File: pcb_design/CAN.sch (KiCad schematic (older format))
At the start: 7 parts, among them U2 ISO1050

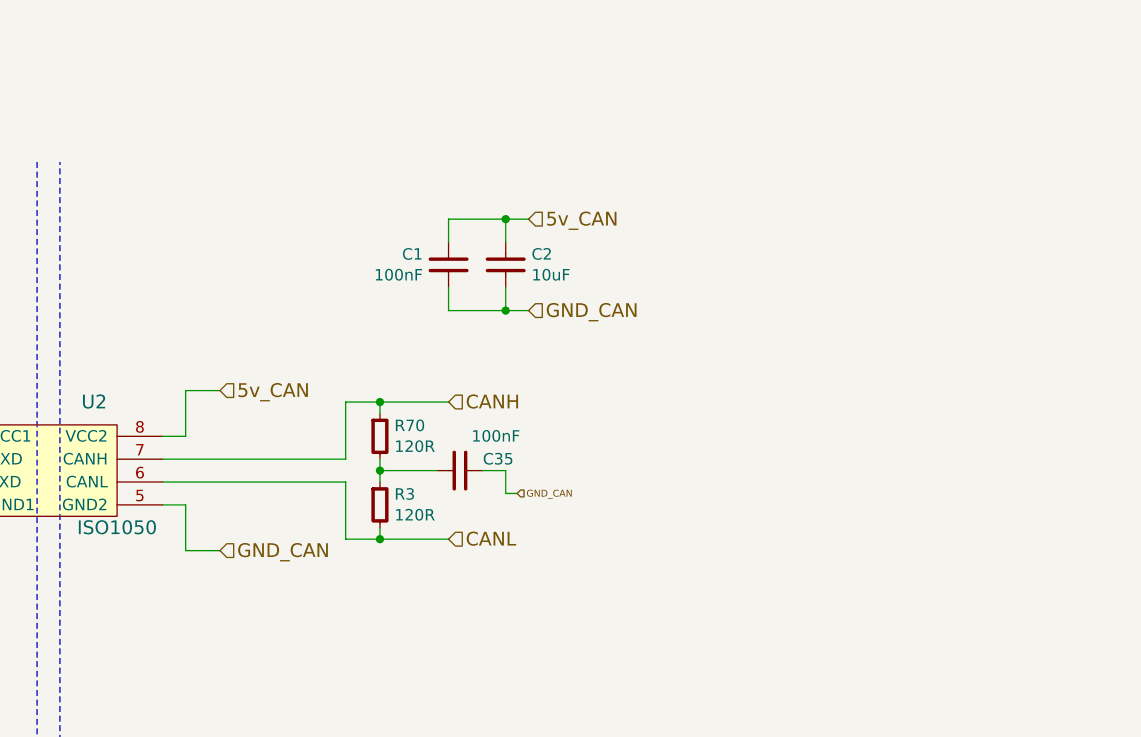
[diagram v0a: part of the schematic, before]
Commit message: Added reverse polarity protection on the isolated side of CON connector. Also, more layout
Signed-off-by: Marcos Chaparro <mchaparro@paltatech.com>
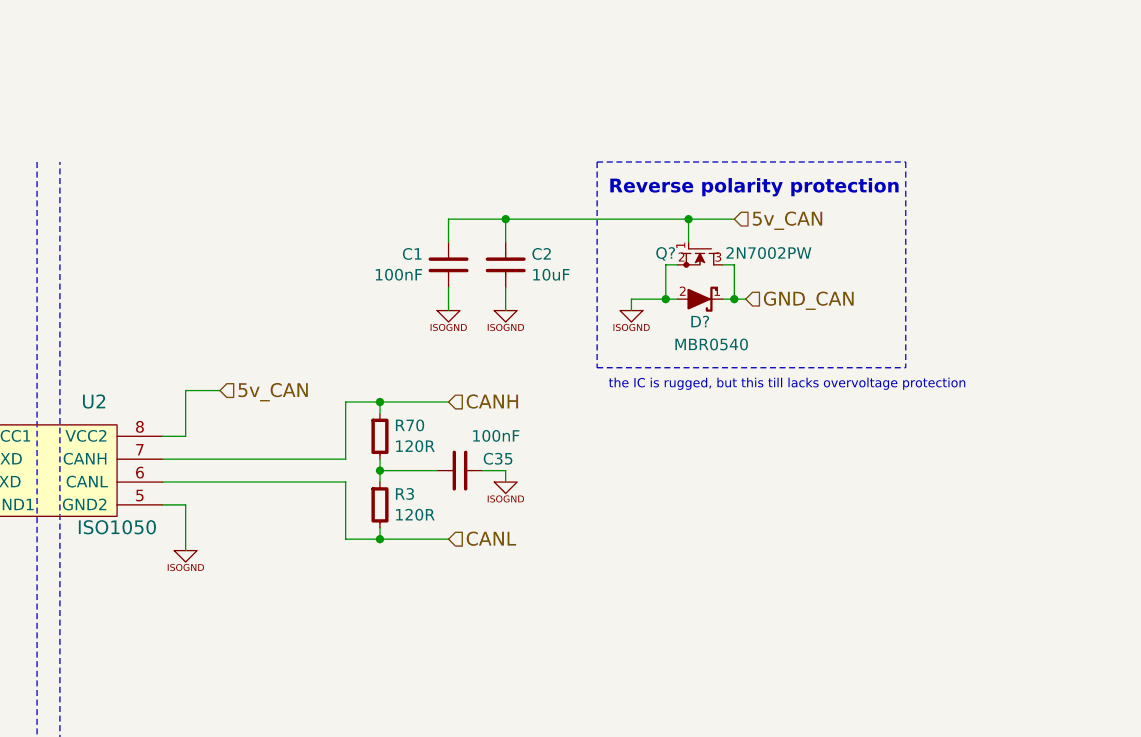
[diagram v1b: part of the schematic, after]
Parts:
- added D?: MBR0540, smd-semi:SOD-123, symbol MBR0540
- added Q?: 2N7002PW, smd-semi:SC-70, symbol 2N7002PW
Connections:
- net 5v_CAN: now also Q?.1 (G)
- net GND_CAN: now also D?.1 (K), Q?.3 (D); no longer C1.2, C2.2, C35.1, U2.5 (GND2)
- new net ISOGND: C1.2, C2.2, C35.1, D?.2 (A), Q?.2 (S), U2.5 (GND2)
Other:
- note added: "Reverse polarity protection"
- note added: "the IC is rugged, but this till lacks overvoltage protection"
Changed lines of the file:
@@
 $EndDescr
 $Comp
-L GND-RESCUE-BLDC_4 #PWR032
+L GND-RESCUE-BLDC_4 #PWR35
 U 1 1 53F59F97
 P 4950 4250
-F 0 "#PWR032" H 4950 4250 30  0001 C CNN
+F 0 "#PWR35" H 4950 4250 30  0001 C CNN
 F 1 "GND" H 4950 4180 30  0001 C CNN
 F 2 "" H 4950 4250 60  0000 C CNN
@@
 $EndComp
 $Comp
-L GND-RESCUE-BLDC_4 #PWR033
+L GND-RESCUE-BLDC_4 #PWR33
 U 1 1 53F59FB0
 P 4000 4250
-F 0 "#PWR033" H 4000 4250 30  0001 C CNN
+F 0 "#PWR33" H 4000 4250 30  0001 C CNN
 F 1 "GND" H 4000 4180 30  0001 C CNN
 F 2 "" H 4000 4250 60  0000 C CNN
@@
 	7500 3050 7500 2950
 Wire Wire Line
-	7250 2950 7600 2950
+	7250 2950 8500 2950
 Wire Wire Line
 	7250 2950 7250 3050
-Text HLabel 7600 2950 2    60   Input ~ 0
+Text HLabel 8500 2950 2    60   Input ~ 0
 5v_CAN
 Wire Wire Line
 	7500 3250 7500 3350
 Wire Wire Line
-	7250 3350 7600 3350
-Wire Wire Line
 	7250 3350 7250 3250
-Text HLabel 7600 3350 2    60   Input ~ 0
-GND_CAN
 Connection ~ 7500 2950
-Connection ~ 7500 3350
-Text HLabel 6250 4400 2    60   Input ~ 0
-GND_CAN
-Wire Wire Line
-	6250 4400 6100 4400
 Wire Wire Line
 	6100 4400 6100 4200
@@
 	7400 4050 7500 4050
 Wire Wire Line
-	7500 4050 7500 4150
-Text HLabel 7550 4150 2    30   Input ~ 0
-GND_CAN
-Wire Wire Line
-	7500 4150 7550 4150
-$Comp
-L +3.3 #PWR034
+	7500 4050 7500 4100
+$Comp
+L +3.3 #PWR32
 U 1 1 588B7BD5
 P 4000 3850
-F 0 "#PWR034" H 0   100 30  0001 C CNN
+F 0 "#PWR32" H 0   100 30  0001 C CNN
 F 1 "+3.3" H 4000 3983 50  0000 C CNN
 F 2 "" H 0   50  60  0000 C CNN
@@
 $EndComp
 $Comp
-L +3.3 #PWR035
+L +3.3 #PWR34
 U 1 1 588B7BFF
 P 4950 3850
-F 0 "#PWR035" H 0   100 30  0001 C CNN
+F 0 "#PWR34" H 0   100 30  0001 C CNN
 F 1 "+3.3" H 4950 3983 50  0000 C CNN
 F 2 "" H 0   50  60  0000 C CNN
@@
 Wire Notes Line
 	5550 5400 5550 2700
+$Comp
+L 2N7002PW Q?
+U 1 1 5890FB52
+P 8350 3100
+F 0 "Q?" V 8350 2950 50  0000 C CNN
+F 1 "2N7002PW" V 8350 3400 50  0000 C CNN
+F 2 "smd-semi:SC-70" H 50  -1000 50  0001 C CNN
+F 3 "http://www.nxp.com/documents/data_sheet/2N7002PW.pdf" H 50  -900 60  0001 C CNN
+F 4 "2N7002PW,115" H 8350 3100 60  0001 C CNN "mfg#"
+F 5 "NMOS NXP 2N7002PW" H 50  -1100 60  0001 C CNN "BOM"
+	1    8350 3100
+	0    1    1    0
+$EndComp
+Text HLabel 8550 3300 2    60   Input ~ 0
+GND_CAN
+Wire Wire Line
+	8450 3300 8550 3300
+$Comp
+L ISOGND #PWR?
+U 1 1 5890FDF1
+P 8050 3350
+F 0 "#PWR?" H 8100 3400 30  0001 C CNN
+F 1 "ISOGND" H -1350 50  30  0001 C CNN
+F 2 "" H -1350 50  60  0000 C CNN
+F 3 "" H -1350 50  60  0000 C CNN
+	1    8050 3350
+	-1   0    0    -1
+$EndComp
+$Comp
+L ISOGND #PWR?
+U 1 1 5890FE5B
+P 7250 3350
+F 0 "#PWR?" H 7300 3400 30  0001 C CNN
+F 1 "ISOGND" H -2150 50  30  0001 C CNN
+F 2 "" H -2150 50  60  0000 C CNN
+F 3 "" H -2150 50  60  0000 C CNN
+	1    7250 3350
+	1    0    0    -1
+$EndComp
+$Comp
+L ISOGND #PWR?
+U 1 1 5890FE96
+P 7500 3350
+F 0 "#PWR?" H 7550 3400 30  0001 C CNN
+F 1 "ISOGND" H -1900 50  30  0001 C CNN
+F 2 "" H -1900 50  60  0000 C CNN
+F 3 "" H -1900 50  60  0000 C CNN
+	1    7500 3350
+	1    0    0    -1
+$EndComp
+$Comp
+L ISOGND #PWR?
+U 1 1 5890FF21
+P 6100 4400
+F 0 "#PWR?" H 6150 4450 30  0001 C CNN
+F 1 "ISOGND" H -3300 1100 30  0001 C CNN
+F 2 "" H -3300 1100 60  0000 C CNN
+F 3 "" H -3300 1100 60  0000 C CNN
+	1    6100 4400
+	1    0    0    -1
+$EndComp
+Wire Wire Line
+	8050 3350 8050 3300
+Wire Wire Line
+	8050 3300 8250 3300
+Connection ~ 8300 2950
+Wire Wire Line
+	8300 3050 8300 2950
+$Comp
+L MBR0540 D?
+U 1 1 5891137A
+P 8350 3300
+F 0 "D?" V 8250 3300 50  0000 C CNN
+F 1 "MBR0540" V 8150 3250 50  0000 C CNN
+F 2 "smd-semi:SOD-123" H 200 -250 50  0001 C CNN
+F 3 "http://www.onsemi.com/pub_link/Collateral/MBR0540T1-D.PDF" H 200 -150 60  0001 C CNN
+F 4 "SCHOTTKY MBR0540" H 200 -350 60  0001 C CNN "BOM"
+	1    8350 3300
+	0    -1   -1   0
+$EndComp
+Wire Wire Line
+	8250 3150 8200 3150
+Wire Wire Line
+	8200 3150 8200 3300
+Connection ~ 8200 3300
+Wire Wire Line
+	8450 3150 8500 3150
+Wire Wire Line
+	8500 3150 8500 3300
+Connection ~ 8500 3300
+Wire Notes Line
+	7900 2700 7900 3600
+Wire Notes Line
+	7900 3600 9250 3600
+Text Notes 7950 2850 0    60   ~ 12
+Reverse polarity protection
+Wire Notes Line
+	7900 2700 9250 2700
+Wire Notes Line
+	9250 2700 9250 3600
+Text Notes 7950 3700 0    40   ~ 0
+the IC is rugged, but this till lacks overvoltage protection
+$Comp
+L ISOGND #PWR?
+U 1 1 58911D5C
+P 7500 4100
+F 0 "#PWR?" H 7550 4150 30  0001 C CNN
+F 1 "ISOGND" H -1900 800 30  0001 C CNN
+F 2 "" H -1900 800 60  0000 C CNN
+F 3 "" H -1900 800 60  0000 C CNN
+	1    7500 4100
+	1    0    0    -1
+$EndComp
 $EndSCHEMATC

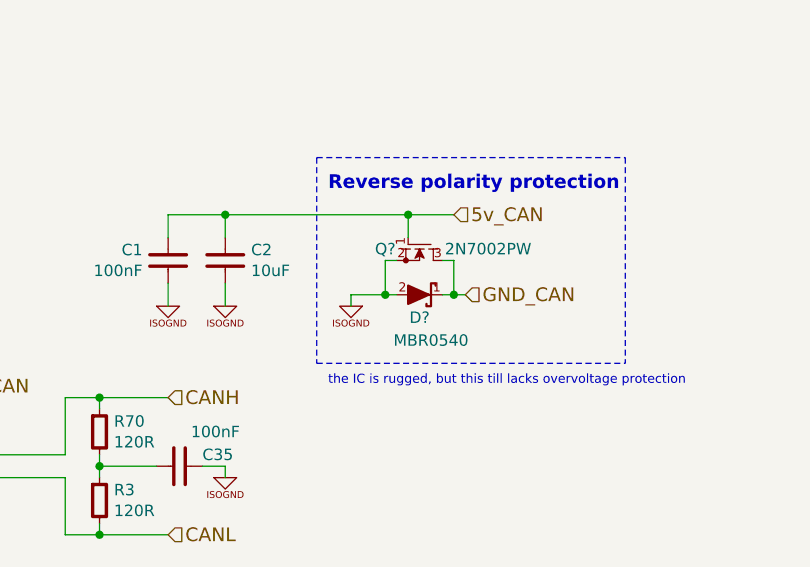
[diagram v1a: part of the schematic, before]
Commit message: Resolver routed using push pull buffer
Signed-off-by: Marcos Chaparro <mchaparro@paltatech.com>
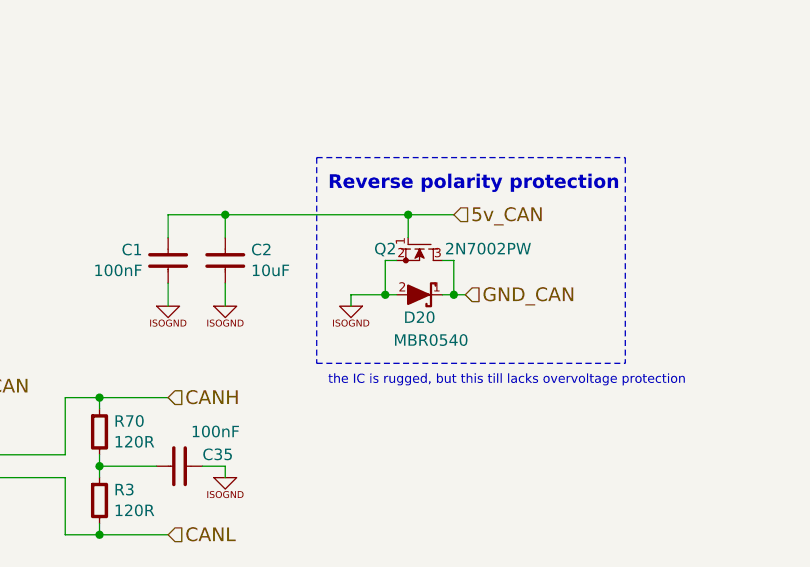
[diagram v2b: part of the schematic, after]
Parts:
- gave numbers to parts that had none: 2
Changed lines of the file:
@@
 $EndDescr
 $Comp
-L GND-RESCUE-BLDC_4 #PWR35
+L GND-RESCUE-BLDC_4 #PWR032
 U 1 1 53F59F97
 P 4950 4250
-F 0 "#PWR35" H 4950 4250 30  0001 C CNN
+F 0 "#PWR032" H 4950 4250 30  0001 C CNN
 F 1 "GND" H 4950 4180 30  0001 C CNN
 F 2 "" H 4950 4250 60  0000 C CNN
@@
 $EndComp
 $Comp
-L GND-RESCUE-BLDC_4 #PWR33
+L GND-RESCUE-BLDC_4 #PWR033
 U 1 1 53F59FB0
 P 4000 4250
-F 0 "#PWR33" H 4000 4250 30  0001 C CNN
+F 0 "#PWR033" H 4000 4250 30  0001 C CNN
 F 1 "GND" H 4000 4180 30  0001 C CNN
 F 2 "" H 4000 4250 60  0000 C CNN
@@
 	7500 4050 7500 4100
 $Comp
-L +3.3 #PWR32
+L +3.3 #PWR034
 U 1 1 588B7BD5
 P 4000 3850
-F 0 "#PWR32" H 0   100 30  0001 C CNN
+F 0 "#PWR034" H 0   100 30  0001 C CNN
 F 1 "+3.3" H 4000 3983 50  0000 C CNN
 F 2 "" H 0   50  60  0000 C CNN
@@
 $EndComp
 $Comp
-L +3.3 #PWR34
+L +3.3 #PWR035
 U 1 1 588B7BFF
 P 4950 3850
-F 0 "#PWR34" H 0   100 30  0001 C CNN
+F 0 "#PWR035" H 0   100 30  0001 C CNN
 F 1 "+3.3" H 4950 3983 50  0000 C CNN
 F 2 "" H 0   50  60  0000 C CNN
@@
 	5550 5400 5550 2700
 $Comp
-L 2N7002PW Q?
+L 2N7002PW Q2
 U 1 1 5890FB52
 P 8350 3100
-F 0 "Q?" V 8350 2950 50  0000 C CNN
+F 0 "Q2" V 8350 2950 50  0000 C CNN
 F 1 "2N7002PW" V 8350 3400 50  0000 C CNN
 F 2 "smd-semi:SC-70" H 50  -1000 50  0001 C CNN
@@
 	8450 3300 8550 3300
 $Comp
-L ISOGND #PWR?
+L ISOGND #PWR036
 U 1 1 5890FDF1
 P 8050 3350
-F 0 "#PWR?" H 8100 3400 30  0001 C CNN
+F 0 "#PWR036" H 8100 3400 30  0001 C CNN
 F 1 "ISOGND" H -1350 50  30  0001 C CNN
 F 2 "" H -1350 50  60  0000 C CNN
@@
 $EndComp
 $Comp
-L ISOGND #PWR?
+L ISOGND #PWR037
 U 1 1 5890FE5B
 P 7250 3350
-F 0 "#PWR?" H 7300 3400 30  0001 C CNN
+F 0 "#PWR037" H 7300 3400 30  0001 C CNN
 F 1 "ISOGND" H -2150 50  30  0001 C CNN
 F 2 "" H -2150 50  60  0000 C CNN
@@
 $EndComp
 $Comp
-L ISOGND #PWR?
+L ISOGND #PWR038
 U 1 1 5890FE96
 P 7500 3350
-F 0 "#PWR?" H 7550 3400 30  0001 C CNN
+F 0 "#PWR038" H 7550 3400 30  0001 C CNN
 F 1 "ISOGND" H -1900 50  30  0001 C CNN
 F 2 "" H -1900 50  60  0000 C CNN
@@
 $EndComp
 $Comp
-L ISOGND #PWR?
+L ISOGND #PWR039
 U 1 1 5890FF21
 P 6100 4400
-F 0 "#PWR?" H 6150 4450 30  0001 C CNN
+F 0 "#PWR039" H 6150 4450 30  0001 C CNN
 F 1 "ISOGND" H -3300 1100 30  0001 C CNN
 F 2 "" H -3300 1100 60  0000 C CNN
@@
 	8300 3050 8300 2950
 $Comp
-L MBR0540 D?
+L MBR0540 D20
 U 1 1 5891137A
 P 8350 3300
-F 0 "D?" V 8250 3300 50  0000 C CNN
+F 0 "D20" V 8250 3300 50  0000 C CNN
 F 1 "MBR0540" V 8150 3250 50  0000 C CNN
 F 2 "smd-semi:SOD-123" H 200 -250 50  0001 C CNN
@@
 the IC is rugged, but this till lacks overvoltage protection
 $Comp
-L ISOGND #PWR?
+L ISOGND #PWR040
 U 1 1 58911D5C
 P 7500 4100
-F 0 "#PWR?" H 7550 4150 30  0001 C CNN
+F 0 "#PWR040" H 7550 4150 30  0001 C CNN
 F 1 "ISOGND" H -1900 800 30  0001 C CNN
 F 2 "" H -1900 800 60  0000 C CNN

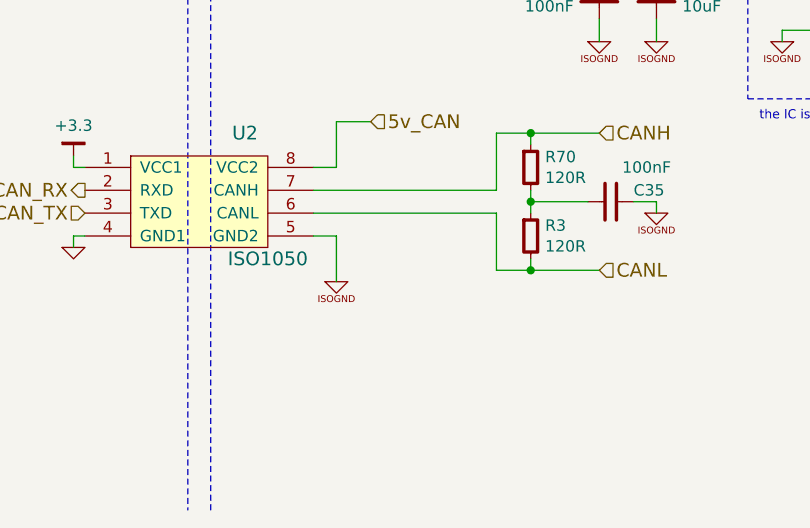
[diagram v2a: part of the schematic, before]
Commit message: Routing complete. Added 3D models. No DRC errors, a few ERC warnings
Signed-off-by: Marcos Chaparro <mchaparro@paltatech.com>
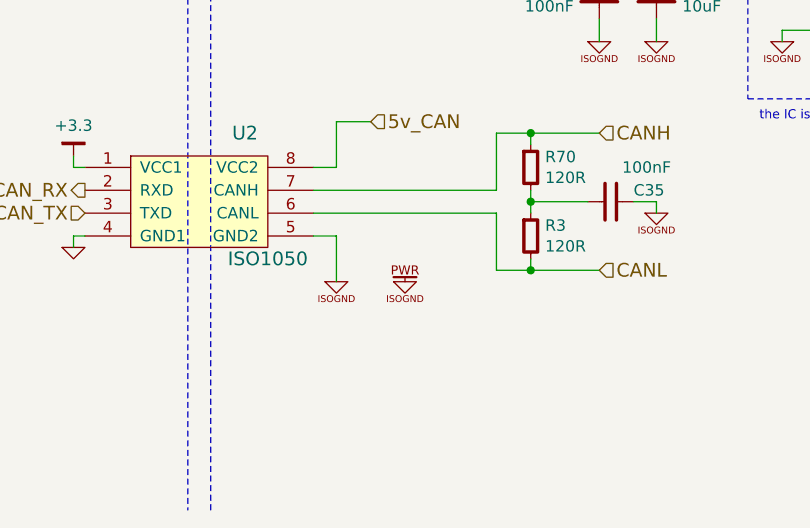
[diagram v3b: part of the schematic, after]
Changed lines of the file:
@@
 $EndDescr
 $Comp
-L GND-RESCUE-BLDC_4 #PWR032
+L GND-RESCUE-BLDC_4 #PWR035
 U 1 1 53F59F97
 P 4950 4250
-F 0 "#PWR032" H 4950 4250 30  0001 C CNN
+F 0 "#PWR035" H 4950 4250 30  0001 C CNN
 F 1 "GND" H 4950 4180 30  0001 C CNN
 F 2 "" H 4950 4250 60  0000 C CNN
@@
 $EndComp
 $Comp
-L GND-RESCUE-BLDC_4 #PWR033
+L GND-RESCUE-BLDC_4 #PWR036
 U 1 1 53F59FB0
 P 4000 4250
-F 0 "#PWR033" H 4000 4250 30  0001 C CNN
+F 0 "#PWR036" H 4000 4250 30  0001 C CNN
 F 1 "GND" H 4000 4180 30  0001 C CNN
 F 2 "" H 4000 4250 60  0000 C CNN
@@
 	7500 4050 7500 4100
 $Comp
-L +3.3 #PWR034
+L +3.3 #PWR037
 U 1 1 588B7BD5
 P 4000 3850
-F 0 "#PWR034" H 0   100 30  0001 C CNN
+F 0 "#PWR037" H 0   100 30  0001 C CNN
 F 1 "+3.3" H 4000 3983 50  0000 C CNN
 F 2 "" H 0   50  60  0000 C CNN
@@
 $EndComp
 $Comp
-L +3.3 #PWR035
+L +3.3 #PWR038
 U 1 1 588B7BFF
 P 4950 3850
-F 0 "#PWR035" H 0   100 30  0001 C CNN
+F 0 "#PWR038" H 0   100 30  0001 C CNN
 F 1 "+3.3" H 4950 3983 50  0000 C CNN
 F 2 "" H 0   50  60  0000 C CNN
@@
 	8450 3300 8550 3300
 $Comp
-L ISOGND #PWR036
+L ISOGND #PWR039
 U 1 1 5890FDF1
 P 8050 3350
-F 0 "#PWR036" H 8100 3400 30  0001 C CNN
+F 0 "#PWR039" H 8100 3400 30  0001 C CNN
 F 1 "ISOGND" H -1350 50  30  0001 C CNN
 F 2 "" H -1350 50  60  0000 C CNN
@@
 $EndComp
 $Comp
-L ISOGND #PWR037
+L ISOGND #PWR040
 U 1 1 5890FE5B
 P 7250 3350
-F 0 "#PWR037" H 7300 3400 30  0001 C CNN
+F 0 "#PWR040" H 7300 3400 30  0001 C CNN
 F 1 "ISOGND" H -2150 50  30  0001 C CNN
 F 2 "" H -2150 50  60  0000 C CNN
@@
 $EndComp
 $Comp
-L ISOGND #PWR038
+L ISOGND #PWR041
 U 1 1 5890FE96
 P 7500 3350
-F 0 "#PWR038" H 7550 3400 30  0001 C CNN
+F 0 "#PWR041" H 7550 3400 30  0001 C CNN
 F 1 "ISOGND" H -1900 50  30  0001 C CNN
 F 2 "" H -1900 50  60  0000 C CNN
@@
 $EndComp
 $Comp
-L ISOGND #PWR039
+L ISOGND #PWR042
 U 1 1 5890FF21
 P 6100 4400
-F 0 "#PWR039" H 6150 4450 30  0001 C CNN
+F 0 "#PWR042" H 6150 4450 30  0001 C CNN
 F 1 "ISOGND" H -3300 1100 30  0001 C CNN
 F 2 "" H -3300 1100 60  0000 C CNN
@@
 the IC is rugged, but this till lacks overvoltage protection
 $Comp
-L ISOGND #PWR040
+L ISOGND #PWR043
 U 1 1 58911D5C
 P 7500 4100
-F 0 "#PWR040" H 7550 4150 30  0001 C CNN
+F 0 "#PWR043" H 7550 4150 30  0001 C CNN
 F 1 "ISOGND" H -1900 800 30  0001 C CNN
 F 2 "" H -1900 800 60  0000 C CNN
@@
 	1    0    0    -1
 $EndComp
+$Comp
+L PWR_FLAG #PWR044
+U 1 1 5893E2D5
+P 6400 4400
+F 0 "#PWR044" H 6450 4450 50  0001 C CNN
+F 1 "PWR_FLAG" H -1350 300 50  0001 C CNN
+F 2 "" H -1350 300 60  0000 C CNN
+F 3 "" H -1350 300 60  0000 C CNN
+	1    6400 4400
+	1    0    0    -1
+$EndComp
+$Comp
+L ISOGND #PWR045
+U 1 1 5893E31D
+P 6400 4400
+F 0 "#PWR045" H 6450 4450 30  0001 C CNN
+F 1 "ISOGND" H -3000 1100 30  0001 C CNN
+F 2 "" H -3000 1100 60  0000 C CNN
+F 3 "" H -3000 1100 60  0000 C CNN
+	1    6400 4400
+	1    0    0    -1
+$EndComp

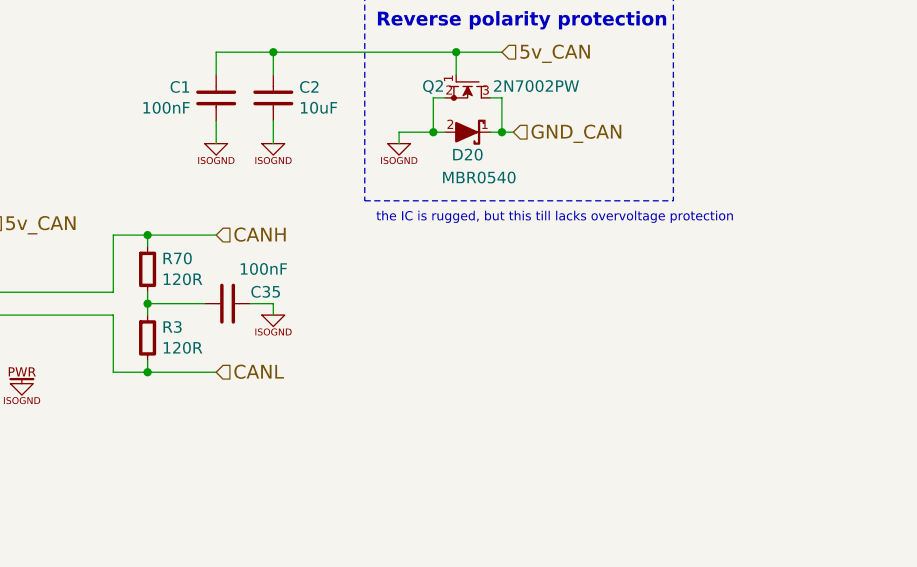
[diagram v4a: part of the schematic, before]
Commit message: Updated component values according to simulations. 1.5khz for user inputs and  240khz lp pass filters for motor control
Signed-off-by: Marcos Chaparro <mchaparro@paltatech.com>
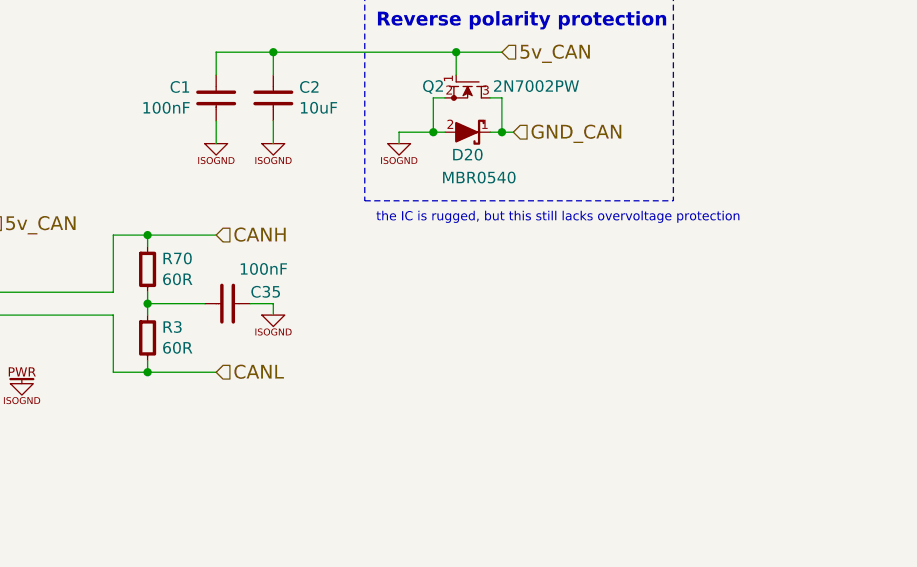
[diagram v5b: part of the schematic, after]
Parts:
- R3, R70: value 120R -> 60R; BOM RES SMD 1k 5% [0603] -> RES SMD 60 Ohm 1% [0603]
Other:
- note added: "the IC is rugged, but this still lacks overvoltage protection"
- note removed: "the IC is rugged, but this till lacks overvoltage protection"
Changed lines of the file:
@@
 P 6950 4200
 F 0 "R3" H 7013 4246 50  0000 L CNN
-F 1 "120R" H 7013 4155 50  0000 L CNN
+F 1 "60R" H 7013 4155 50  0000 L CNN
 F 2 "IPC7351-Nominal:RESC1608X50" H 6950 4200 50  0001 C CNN
 F 3 "" H 6950 4250 60  0000 C CNN
-F 4 "RES SMD 1k 5% [0603]" H 7700 4750 60  0001 C CNN "BOM"
+F 4 "RES SMD 60 Ohm 1% [0603]" H 7700 4750 60  0001 C CNN "BOM"
 	1    6950 4200
 	1    0    0    -1
@@
 P 6950 3900
 F 0 "R70" H 7013 3946 50  0000 L CNN
-F 1 "120R" H 7013 3855 50  0000 L CNN
+F 1 "60R" H 7013 3855 50  0000 L CNN
 F 2 "IPC7351-Nominal:RESC1608X50" H 6950 3900 50  0001 C CNN
 F 3 "" H 6950 3950 60  0000 C CNN
-F 4 "RES SMD 1k 5% [0603]" H 7700 4450 60  0001 C CNN "BOM"
+F 4 "RES SMD 60 Ohm 1% [0603]" H 7700 4450 60  0001 C CNN "BOM"
 	1    6950 3900
 	1    0    0    -1
@@
 	9250 2700 9250 3600
 Text Notes 7950 3700 0    40   ~ 0
-the IC is rugged, but this till lacks overvoltage protection
+the IC is rugged, but this still lacks overvoltage protection
 $Comp
 L ISOGND #PWR48
